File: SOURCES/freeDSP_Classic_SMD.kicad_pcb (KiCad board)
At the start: 2 copper layers, 168 parts, among them J1 RCA_01, J2 RCA_01, J3 CONN_01X02, J4 RCA_01, J5 RCA_01, J6 RCA_01, J7 RCA_01, P1 CONN_01X06, P2 CONN_01X03, P3 CONN_02X05, P4 STDCONN, P5 STDCONN, P6 STDCONN, P7 STDCONN, P8 CONN_02X03, P9 CONN_02X03, Q1 BSS123, Q10 BSH103,215, Q11 BSH103,215, Q12 BSH103,215, Q13 BSH103,215, Q14 MMBF5434, Q15 MMBF5434, Q16 MMBF5434, Q17 MMBF5434, Q18 BSS123, Q2 BSS123, Q3 BSS123, Q4 BSS123, Q5 FZT751TA, Q6 BSH103,215, Q7 BSH103,215, Q8 BSH103,215, Q9 BSH103,215, SW1 SW_PUSH, U1 ADAU1701, U2 24AA256SN, U3 LME49721, U4 LME49721, U5 SN74LVC3G14, U6 LM393, U7 IDT2305NZ, X1 ASV-24.576MHz-EJ-T

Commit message: layout: placed some components
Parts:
- moved Q13 289.9 mm to (259.7, 128.9)
- moved Q18 282.7 mm to (233.3, 159.7)
- moved Q17 270.8 mm to (228.1, 146.0)
- moved Q15 268.8 mm to (220.5, 153.7)
- moved Q16 264.9 mm to (200.9, 172.6)
- moved Q9 263.6 mm to (219.1, 146.6)
- moved Q4 263.3 mm to (248.6, 86.7)
- moved Q14 261.8 mm to (204.9, 163.0)
- moved Q6 261.5 mm to (211.6, 153.7)
- moved Q10 260.5 mm to (221.6, 137.0)
- moved Q3 259.0 mm to (241.6, 93.4)
- moved Q7 258.1 mm to (191.9, 172.6)
- moved Q11 256.5 mm to (195.9, 165.6)
- moved Q8 255.7 mm to (209.5, 146.6)
- moved Q12 255.1 mm to (202.0, 155.9)
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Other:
- net class Default: clearance 0.2 -> 0.3; trace_width 0.25 -> 0.3
- net class Supply added: clearance 0.3, trace_width 0.6, via_dia 0.6, via_drill 0.4
- rule trace_clearance: 0.2 -> 0.3

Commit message: updated pcb
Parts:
- removed C_res4: x, fdsp_capacitor:C_Radial_D5_L11_P2
- added REF**: MountingHole_3.2mm_M3_ISO14580, fdsp_drillhole:MountingHole_3.2mm_M3_ISO14580, F.Cu at (67.6, 154.2)
- added REF**: MountingHole_3.2mm_M3_ISO14580, fdsp_drillhole:MountingHole_3.2mm_M3_ISO14580, F.Cu at (140.0, 154.2)
- added REF**: MountingHole_3.2mm_M3_ISO14580, fdsp_drillhole:MountingHole_3.2mm_M3_ISO14580, F.Cu at (140.0, 61.5)
- added REF**: MountingHole_3.2mm_M3_ISO14580, fdsp_drillhole:MountingHole_3.2mm_M3_ISO14580, F.Cu at (67.8, 61.7)
- moved Q13 141.1 mm to (130.6, 72.1)
- moved U5 126.3 mm to (99.3, 69.1)
- moved Q17 124.5 mm to (130.6, 68.6), turned to 180 degrees
- moved Q9 120.0 mm to (125.0, 72.1)
- moved Q16 113.3 mm to (130.6, 83.8), turned to 180 degrees
- moved D2 111.3 mm to (68.3, 136.7)
- moved Q15 105.1 mm to (130.6, 99.3), turned to 180 degrees
- moved Q8 103.4 mm to (125.0, 87.1)
- moved Q12 99.2 mm to (130.6, 87.1)
- moved Q7 96.7 mm to (125.0, 102.9)
- moved Q6 93.7 mm to (125.0, 117.9)
- moved Q10 93.0 mm to (130.6, 117.9)
- moved Q11 90.6 mm to (130.6, 102.9)
- moved Q14 88.8 mm to (130.6, 114.3), turned to 180 degrees
- moved C_res3 53.8 mm to (79.2, 153.1), turned to 90 degrees
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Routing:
- net GND: track 0.00 -> 72.9 mm, vias 0 -> 5
- net +3V3: track 0.00 -> 40.1 mm
- net Net-(C_res1-Pad1): track 0.00 -> 16.6 mm
- net Net-(Cboot1-Pad1): track 0.00 -> 14.8 mm
- net VIN: track 0.00 -> 9.84 mm
- net +12V: track 0.00 -> 6.52 mm
- net Net-(LM1-Pad3): track 0.00 -> 5.93 mm
- net Net-(Cboot1-Pad2): track 0.00 -> 2.82 mm
- net (no net): vias 0 -> 19
- added copper zone on B.Cu, net GND
- added copper zone on F.Cu, net GND
- added copper zone on F.Cu, net Net-(C_res1-Pad1)
- added copper zone on F.Cu, net Net-(Cboot1-Pad1)

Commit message: pcb update
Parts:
- moved C31 191.3 mm to (115.3, 61.7), turned to 180 degrees
- moved R19 182.2 mm to (102.4, 62.5), turned to 90 degrees
- moved R14 180.0 mm to (99.3, 71.4), turned to 90 degrees
- moved R23 178.8 mm to (115.3, 64.5), turned to 180 degrees
- moved R18 173.6 mm to (104.3, 70.5), turned to 180 degrees
- moved C27 168.6 mm to (110.5, 62.5), turned to 90 degrees
- moved C23 164.5 mm to (105.7, 62.5), turned to 90 degrees
- moved R15 161.1 mm to (99.3, 62.5), turned to 270 degrees
- moved C26 158.4 mm to (104.3, 73.5), turned to 180 degrees
- moved R39 153.8 mm to (102.0, 79.9), turned to 270 degrees
- moved D9 153.6 mm to (106.0, 94.9)
- moved C52 152.2 mm to (99.9, 97.7)
- moved D6 151.2 mm to (105.0, 86.2), turned to 90 degrees
- moved C30 150.8 mm to (117.3, 69.6), turned to 90 degrees
- moved C53 147.3 mm to (99.9, 92.1)
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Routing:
- net GND: track 72.9 -> 246.5 mm
- net +3V3: track 40.1 -> 86.4 mm
- net 3.3V_SW: track 0.00 -> 27.2 mm
- net Net-(C49-Pad1): track 0.00 -> 25.3 mm
- net (no net): track 0.00 -> 24.0 mm
- net Net-(R38-Pad1): track 0.00 -> 22.6 mm
- net -5V_SW: track 0.00 -> 16.2 mm
- net CH3_IN: track 0.00 -> 16.1 mm
- net Net-(C27-Pad2): track 0.00 -> 16.0 mm
- net Net-(C23-Pad1): track 0.00 -> 15.6 mm
- net Net-(J7-Pad1): track 0.00 -> 14.7 mm
- net CH4_IN: track 0.00 -> 14.1 mm
- net Net-(C22-Pad1): track 0.00 -> 11.9 mm
- net Net-(C26-Pad1): track 0.00 -> 10.9 mm
- net Net-(C50-Pad2): track 0.00 -> 10.5 mm
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
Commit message: Filters and Muting Circuit routed
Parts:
- moved R32 250.9 mm to (17.1, 18.0)
- moved C1 250.9 mm to (-8.70, 69.7)
- moved C10 250.9 mm to (5.40, 68.9)
- moved C12 250.9 mm to (-59.2, 32.1)
- moved C13 250.9 mm to (-22.8, 76.2)
- moved C14 250.9 mm to (-52.2, 25.5)
- moved C18 250.9 mm to (-18.9, 69.6)
- moved C2 250.9 mm to (-59.2, 25.5)
- moved C38 250.9 mm to (15.7, 9.86)
- moved C4 250.9 mm to (-22.8, 82.9)
- moved C43 250.9 mm to (-24.0, 150.4)
- moved C44 250.9 mm to (-14.9, 142.3)
- moved C6 250.9 mm to (-52.2, 32.1)
- moved C9 250.9 mm to (-59.2, 38.8)
- moved D1 250.9 mm to (-26.1, 65.9)
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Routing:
- net GND: track 246.5 -> 418.8 mm, vias 5 -> 7
- net 3.3V_SW: track 27.2 -> 150.0 mm, vias 0 -> 4
- net -5V_SW: track 16.2 -> 95.1 mm, vias 0 -> 3
- net +3V3: track 86.4 -> 163.6 mm, vias 0 -> 1
- net (no net): track 24.0 -> 0.11 mm
- net Net-(C25-Pad2): track 0.00 -> 19.3 mm
- net Net-(C21-Pad1): track 0.00 -> 18.0 mm
- net Net-(C29-Pad1): track 0.00 -> 17.1 mm
- net CH1_IN: track 0.00 -> 15.3 mm
- net Net-(J5-Pad1): track 0.00 -> 14.0 mm
- net Net-(C20-Pad1): track 0.00 -> 13.7 mm
- net CH2_IN: track 0.00 -> 13.6 mm
- net Net-(C31-Pad1): track 8.01 -> 19.0 mm
- net Net-(C28-Pad1): track 0.00 -> 10.8 mm
- net Net-(C25-Pad1): track 0.00 -> 9.28 mm
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
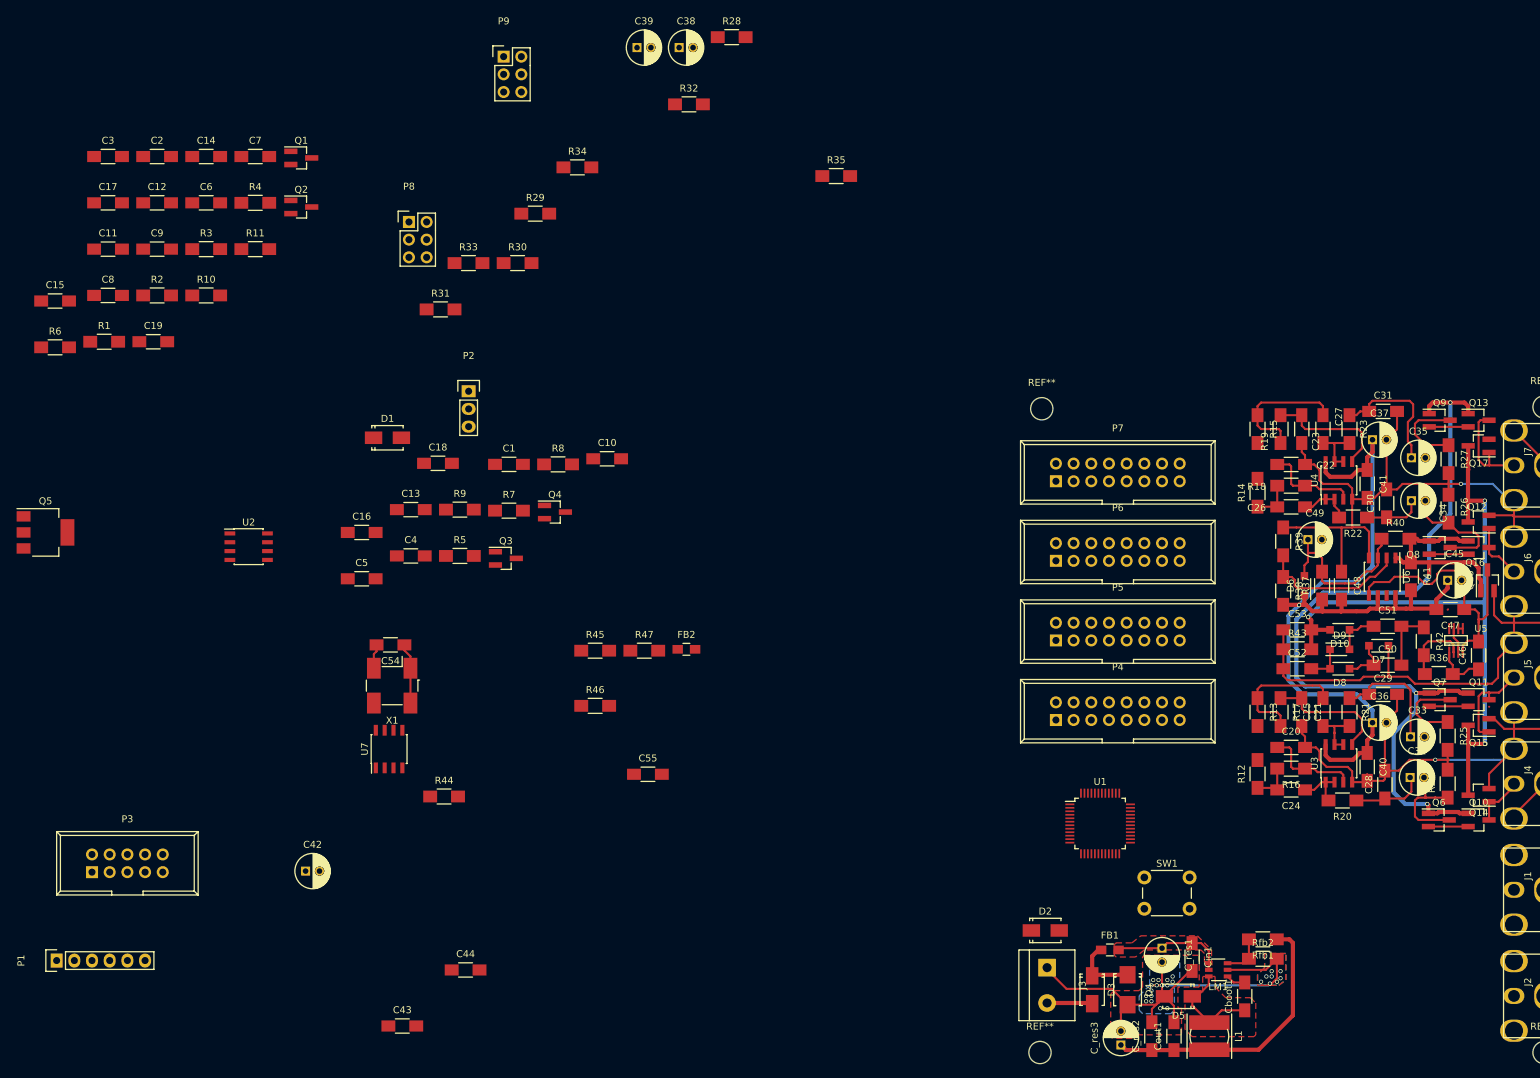
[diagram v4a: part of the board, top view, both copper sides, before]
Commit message: fixed switched GND Q18, placed some components
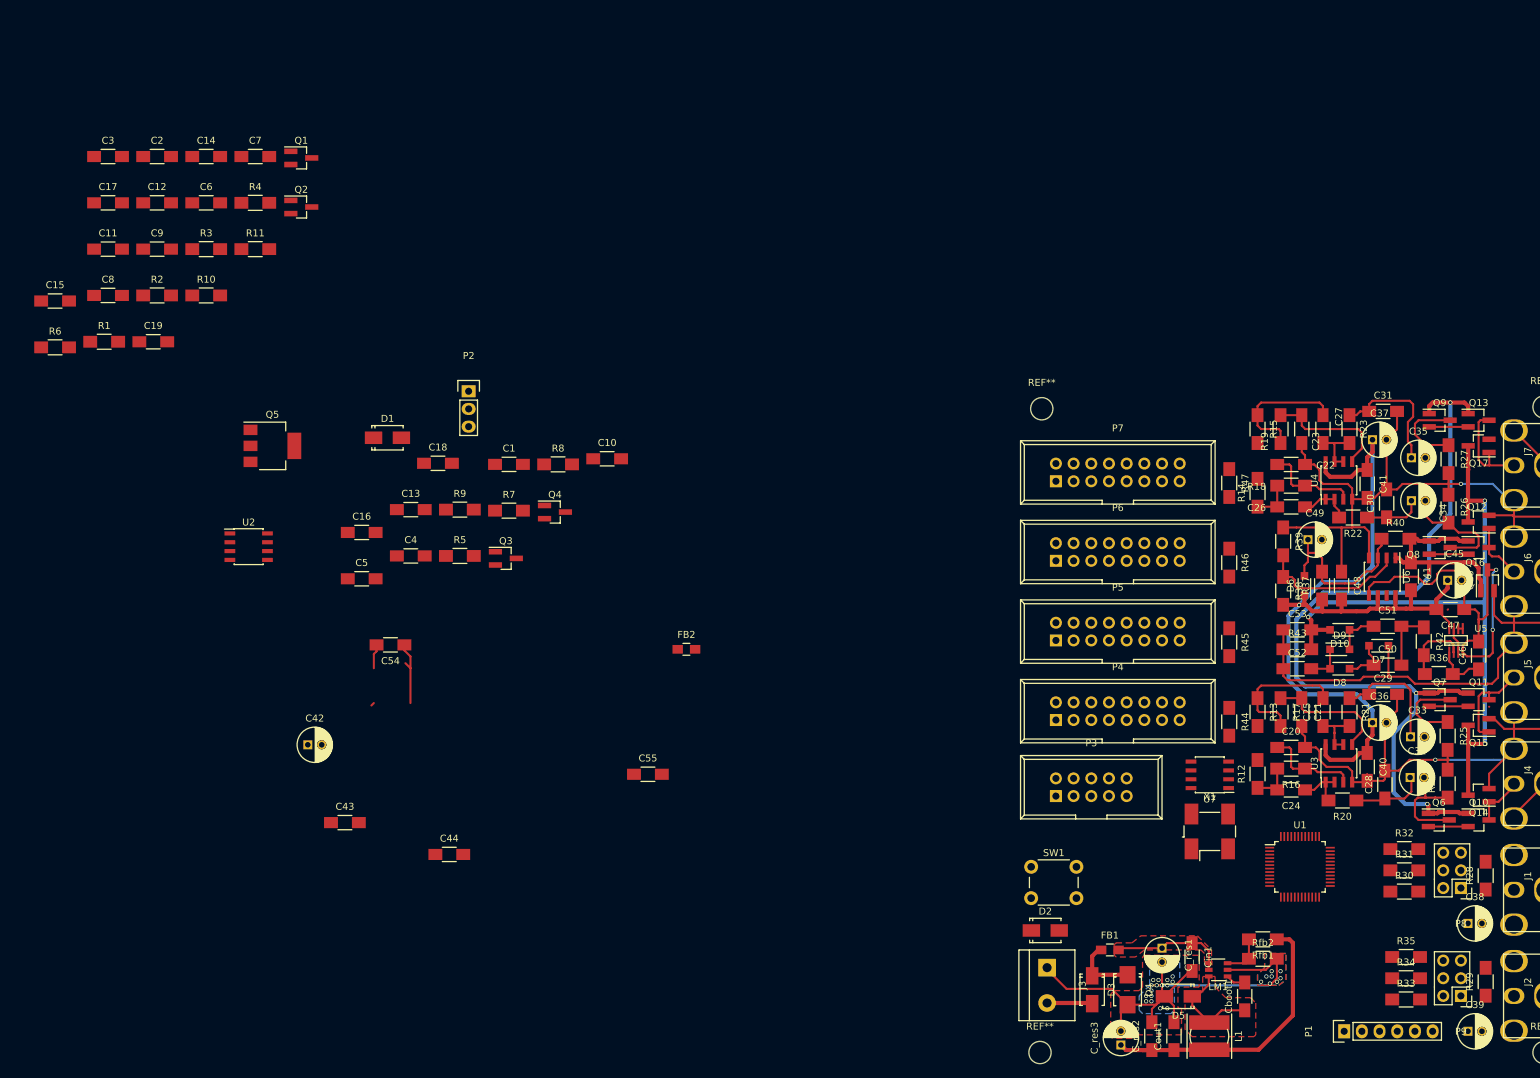
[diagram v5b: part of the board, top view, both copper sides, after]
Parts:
- moved P9 192.6 mm to (128.0, 146.1), turned to 180 degrees
- moved P1 185.2 mm to (111.3, 151.1)
- moved C39 184.9 mm to (129.0, 151.1)
- moved P8 178.8 mm to (128.0, 130.6), turned to 180 degrees
- moved R29 175.5 mm to (131.6, 144.0), turned to 90 degrees
- moved R33 171.2 mm to (120.1, 146.6)
- moved C38 169.3 mm to (129.0, 135.6)
- moved R34 166.5 mm to (120.1, 143.5)
- moved R28 161.9 mm to (131.6, 128.8), turned to 90 degrees
- moved R31 160.1 mm to (119.9, 128.0)
- moved R30 156.1 mm to (119.9, 131.1)
- moved R32 148.3 mm to (119.9, 125.0)
- moved P3 138.9 mm to (69.8, 117.3)
- moved R35 138.8 mm to (120.1, 140.5)
- moved X1 119.3 mm to (91.9, 122.4), turned to 0 degrees
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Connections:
- Q18 pad 3: GND -> /Muting Circuit/GND_SW
- U5 pad 4: GND -> /Muting Circuit/GND_SW
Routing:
- net /Muting Circuit/GND_SW: track 0.00 -> 25.5 mm, vias 0 -> 2
- net GND: track 418.8 -> 411.4 mm
- net +3V3: track 163.6 -> 168.4 mm

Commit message: further routing
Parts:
- moved C19 202.5 mm to (123.8, 137.7)
- moved R6 195.6 mm to (109.6, 120.7), turned to 90 degrees
- moved C3 190.2 mm to (98.4, 120.7), turned to 270 degrees
- moved R11 189.9 mm to (116.9, 137.7), turned to 180 degrees
- moved Q1 185.7 mm to (108.2, 139.4)
- moved C11 180.7 mm to (87.8, 133.1), turned to 90 degrees
- moved R10 172.2 mm to (96.5, 132.3), turned to 90 degrees
- moved Q5 166.6 mm to (114.7, 121.5), turned to 270 degrees
- moved R1 159.8 mm to (75.4, 125.0), turned to 90 degrees
- moved C18 157.0 mm to (123.8, 135.2)
- moved U2 147.5 mm to (92.3, 132.7), turned to 90 degrees
- moved C4 134.7 mm to (106.6, 120.5), turned to 270 degrees
- moved R9 121.6 mm to (95.5, 125.2), turned to 90 degrees
- moved C54 119.3 mm to (89.3, 127.3)
- moved P2 119.2 mm to (78.0, 134.4), turned to 90 degrees
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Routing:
- net GND: track 411.4 -> 522.5 mm
- net +12V: track 6.52 -> 101.2 mm
- net SDA: track 0.00 -> 87.4 mm
- net SCL: track 0.00 -> 86.0 mm, vias 0 -> 6
- net +3V3: track 168.4 -> 248.5 mm
- net BRD_RST: track 0.00 -> 48.4 mm
- net MCLK4: track 0.00 -> 42.9 mm
- net MCLK3: track 0.00 -> 30.3 mm
- net Net-(C2-Pad1): track 0.00 -> 22.5 mm
- net VIN: track 9.84 -> 32.1 mm
- net MCLK2: track 0.00 -> 17.4 mm
- net Net-(D2-Pad2): track 0.00 -> 16.2 mm
- net Net-(C54-Pad1): track 9.74 -> 25.3 mm
- net Net-(R44-Pad2): track 0.00 -> 15.5 mm
- net Net-(P2-Pad2): track 0.00 -> 15.4 mm
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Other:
- net class Default: trace_width 0.3 -> 0.25

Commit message: layout finished
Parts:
- removed C42: 10u, fdsp_capacitor:C_Radial_D5_L11_P2
- removed C43, C44: 100n, fdsp_capacitor:C_1206_HandSoldering
- removed the REF** at (67.6, 154.2)
- removed the REF** at (140.0, 154.2)
- removed the REF** at (140.0, 61.5)
- removed the REF** at (67.8, 61.7)
- added REF**: MountingHole_3.2mm_M3_DIN965, fdsp_drillhole:MountingHole_3.2mm_M3_DIN965, F.Cu at (67.1, 61.5)
- added REF**: MountingHole_3.2mm_M3_DIN965, fdsp_drillhole:MountingHole_3.2mm_M3_DIN965, F.Cu at (140.0, 61.2)
- added REF**: MountingHole_3.2mm_M3_DIN965, fdsp_drillhole:MountingHole_3.2mm_M3_DIN965, F.Cu at (140.0, 154.7)
- added REF**: MountingHole_3.2mm_M3_DIN965, fdsp_drillhole:MountingHole_3.2mm_M3_DIN965, F.Cu at (67.1, 154.7)
- C14, C2, C5, C7: footprint fdsp_capacitor:C_1206_HandSoldering -> fdsp_capacitor:C_Radial_D5_L11_P2
- moved C15 208.8 mm to (107.4, 149.9), turned to 180 degrees
- moved C17 203.7 mm to (107.7, 138.2)
- moved C7 202.0 mm to (115.1, 148.6), turned to 180 degrees
- moved C12 200.4 mm to (114.0, 132.8), turned to 180 degrees
- moved C14 199.2 mm to (107.2, 145.0)
- moved C8 196.7 mm to (101.3, 148.3), turned to 90 degrees
- moved C9 182.7 mm to (99.1, 130.0), turned to 270 degrees
- moved C6 181.4 mm to (103.6, 125.0)
- moved C2 174.9 mm to (113.8, 127.8), turned to 270 degrees
- moved R2 162.4 mm to (94.5, 97.8), turned to 90 degrees
- moved R3 153.2 mm to (93.7, 85.3), turned to 90 degrees
- moved R4 151.1 mm to (96.3, 85.3), turned to 90 degrees
- moved C16 150.5 mm to (107.7, 140.5)
- moved C13 150.2 mm to (112.3, 142.0), turned to 270 degrees
- moved Q2 145.9 mm to (95.0, 91.4), turned to 90 degrees
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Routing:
- net GND: track 522.5 -> 919.0 mm, vias 7 -> 22
- net BRD_RST: track 48.4 -> 207.6 mm, vias 0 -> 3
- net MP11: track 0.00 -> 136.2 mm, vias 0 -> 4
- net +3V3: track 248.5 -> 376.2 mm, vias 1 -> 6
- net MP10: track 0.00 -> 121.2 mm, vias 0 -> 12
- net WP: track 4.68 -> 114.0 mm, vias 0 -> 7
- net MP9: track 0.00 -> 97.5 mm, vias 0 -> 3
- net MP3: track 0.00 -> 97.3 mm, vias 0 -> 3
- net VOUT3: track 0.00 -> 92.9 mm, vias 0 -> 2
- net VOUT2: track 0.00 -> 87.9 mm, vias 0 -> 2
- net MP2: track 0.00 -> 87.1 mm, vias 0 -> 7
- net MP8: track 0.00 -> 81.2 mm, vias 0 -> 5
- net MP1: track 0.00 -> 80.9 mm, vias 0 -> 7
- net MP7: track 0.00 -> 71.4 mm, vias 0 -> 4
- net SDA: track 87.4 -> 153.1 mm, vias 0 -> 14
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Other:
- net class ADAU added: clearance 0.2, trace_width 0.2, via_dia 0.6, via_drill 0.4

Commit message: added logos and gnd vias, generated gerber files
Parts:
- added G***: LOGO, SOURCES:Logo, B.Cu at (94.7, 124.7)
- added G***: LOGO, SOURCES:Logo_small, F.Cu at (81.5, 62.2)
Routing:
- net GND: track 919.0 -> 1022.5 mm, vias 22 -> 73
- net (no net): vias 12 -> 0
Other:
- board text added: "+"
- board text added: "-"
- board text added: "Max Becker Kai Dehmelt Christoph Schmidt Max Wulf"
- board text added: "www.freedsp.cc"
